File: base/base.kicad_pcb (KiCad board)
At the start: 2 copper layers, 105 x 100 mm, 22 parts, among them J1 FTDI, J2 CONN_01X04, J3 CONN_01X40, SW1 SW_Push, U1 Z80CPU, U2 27C256, U3 7404, U4 55257, U5 7432, U6 16550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

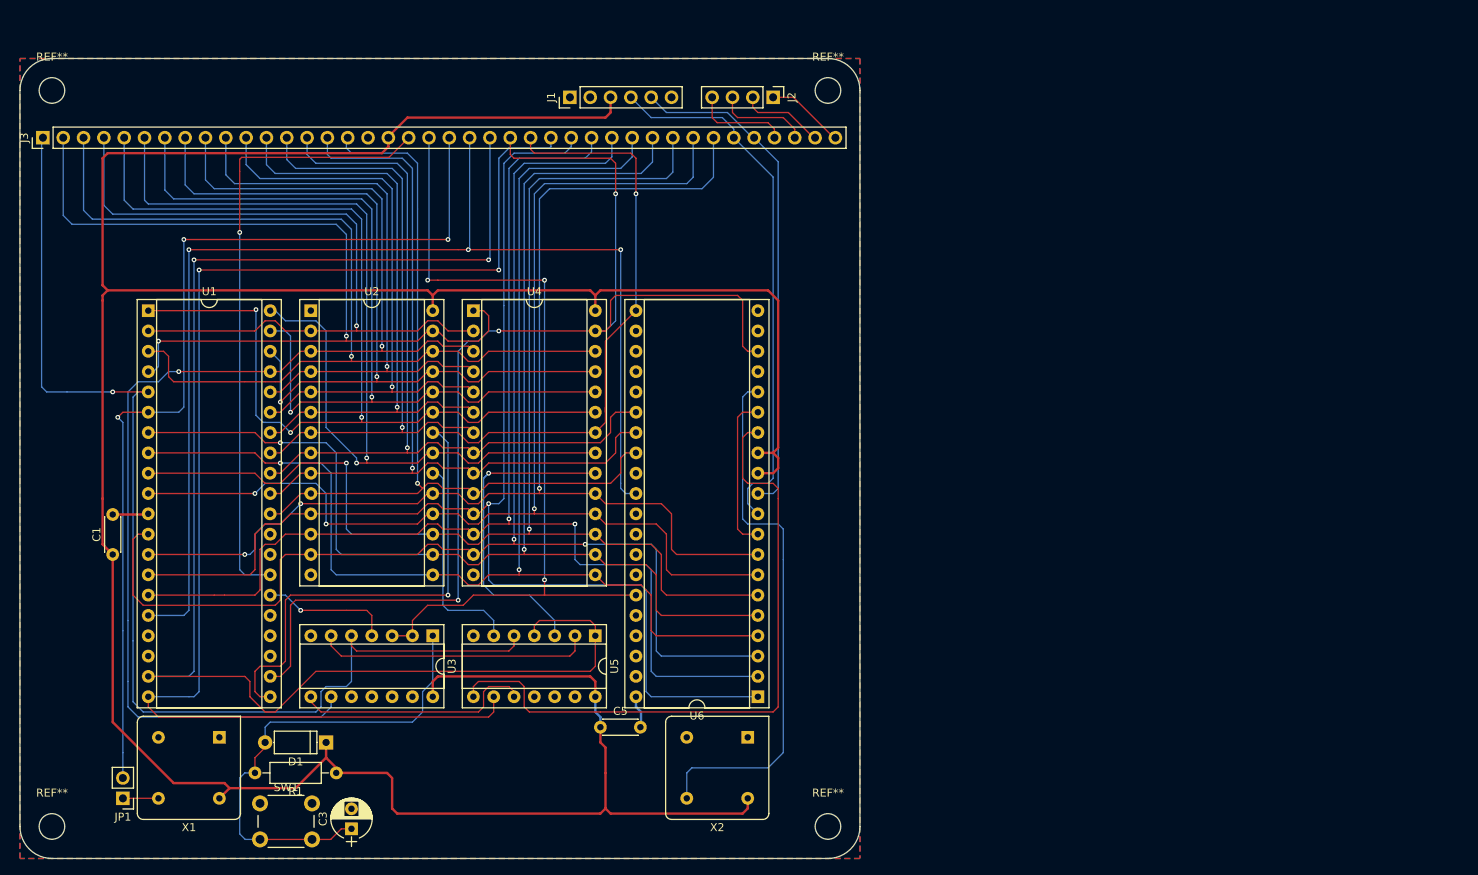
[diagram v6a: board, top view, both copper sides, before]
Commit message: Fixed silkscreen
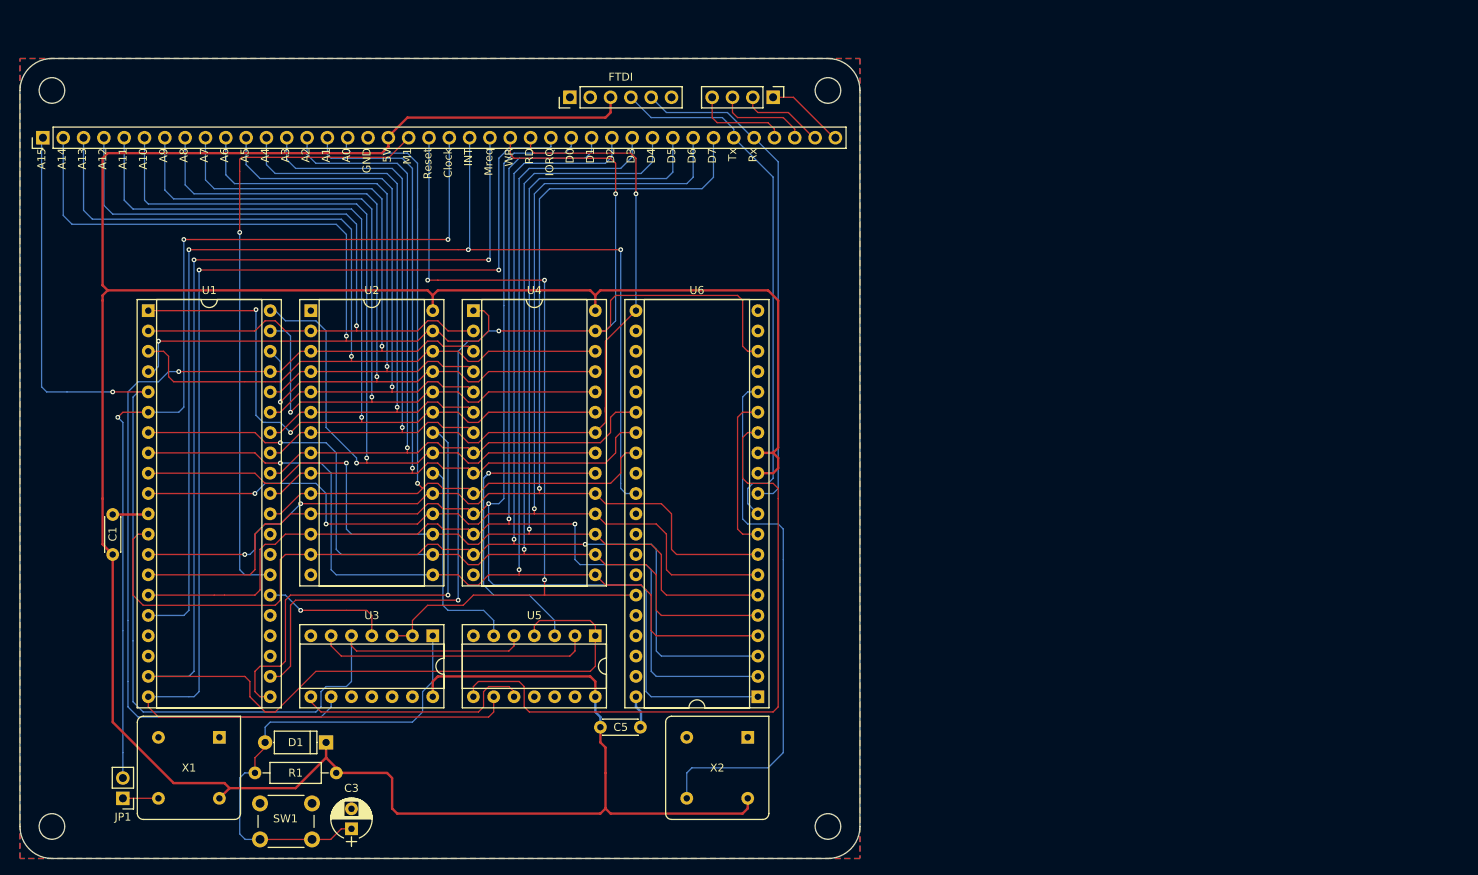
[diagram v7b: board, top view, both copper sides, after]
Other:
- board text added: "5V"
- board text added: "A0"
- board text added: "A1"
- board text added: "A10"
- board text added: "A11"
- board text added: "A12"
- board text added: "A13"
- board text added: "A14"
- board text added: "A15"
- board text added: "A2"
- board text added: "A3"
- board text added: "A4"
- board text added: "A5"
- board text added: "A6"
- board text added: "A7"
- board text added: "A8"
- board text added: "A9"
- board text added: "Clock"
- board text added: "D0"
- board text added: "D1"
- board text added: "D2"
- board text added: "D3"
- board text added: "D4"
- board text added: "D5"
- board text added: "D6"
- board text added: "D7"
- board text added: "GND"
- board text added: "INT"
- board text added: "IORQ"
- board text added: "M1"
- board text added: "Mreq"
- board text added: "RD"
- board text added: "Reset"
- board text added: "Rx"
- board text added: "Tx"
- board text added: "WR"

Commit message: Board layout for remaining pins
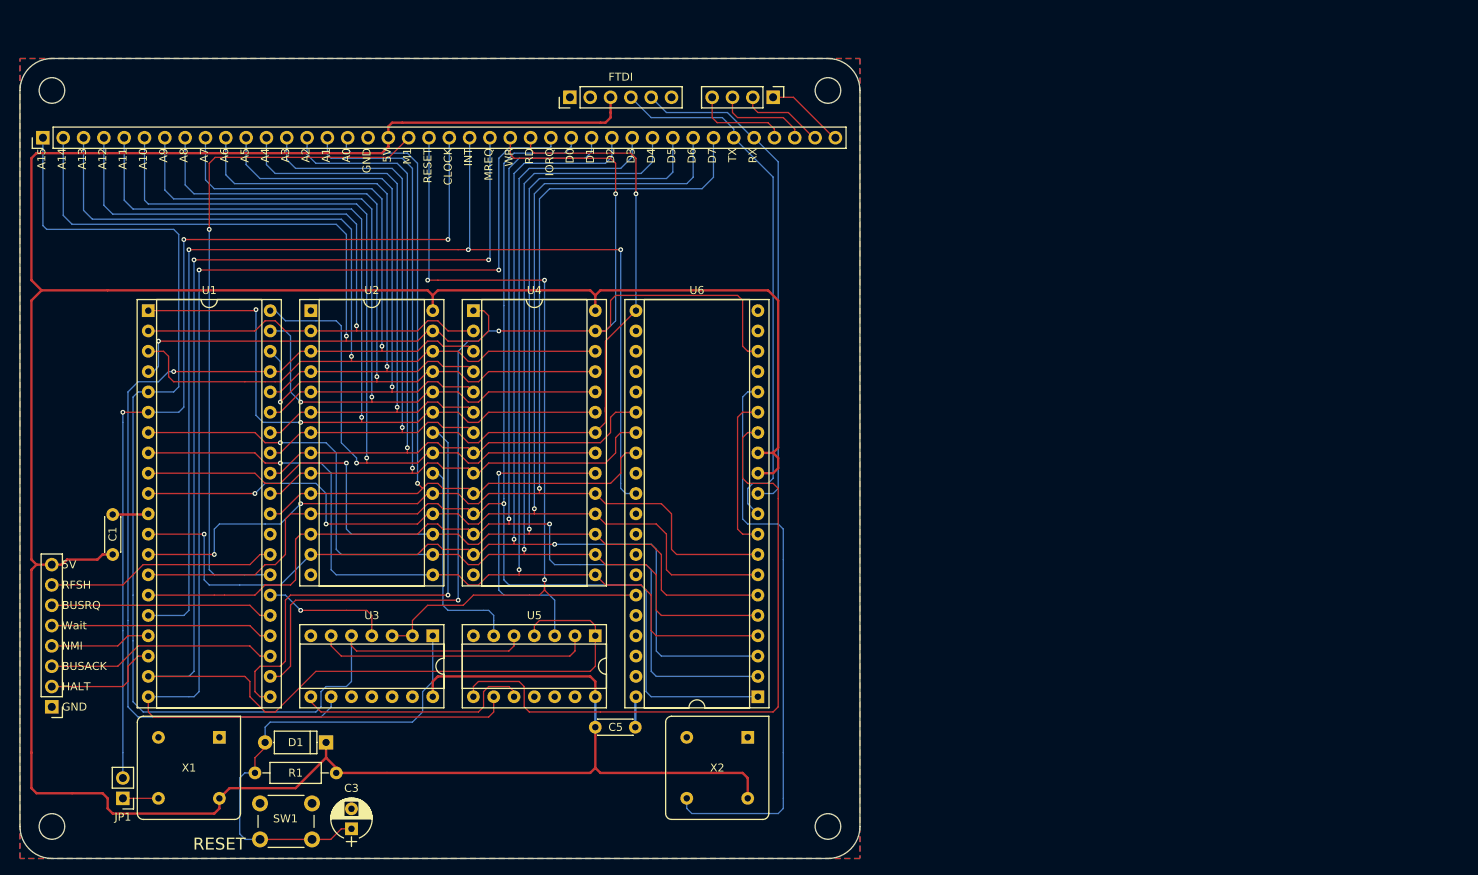
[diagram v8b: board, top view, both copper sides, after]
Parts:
- added J4: CONN_01X08, Pin_Headers:Pin_Header_Straight_1x08_Pitch2.54mm, F.Cu at (54.0, 146.1)
- added REF***: OSHW-Symbol_6.7x6mm_SilkScreen, Symbols:OSHW-Symbol_6.7x6mm_SilkScreen, B.Cu at (104.1, 156.2)
- moved C5 0.64 mm to (121.9, 148.6)
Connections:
- U1 pad 17: Net-(U1-Pad17) -> NMI
- U1 pad 18: Net-(U1-Pad18) -> HALT
- U1 pad 23: Net-(U1-Pad23) -> BUSACK
- U1 pad 24: Net-(U1-Pad24) -> WAIT
- U1 pad 25: Net-(U1-Pad25) -> BUSRQ
- U1 pad 28: Net-(U1-Pad28) -> RFSH
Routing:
- net +5V: track 390.4 -> 428.0 mm
- net RFSH: track 0.00 -> 28.9 mm
- net BUSACK: track 0.00 -> 28.9 mm
- net WAIT: track 0.00 -> 27.8 mm
- net BUSRQ: track 0.00 -> 27.8 mm
- net HALT: track 0.00 -> 14.8 mm
- net NMI: track 0.00 -> 12.6 mm
- net /D2: track 170.0 -> 160.4 mm, vias 2 -> 3
- net M1: track 77.6 -> 84.9 mm
- net /A15: track 145.3 -> 152.3 mm, vias 1 -> 0
- net Net-(U6-Pad16): track 67.2 -> 71.8 mm
- net /A9: track 111.3 -> 108.8 mm
- net RAM_CE: track 41.1 -> 38.6 mm
- net /D0: track 161.0 -> 159.5 mm
- net /A10: track 125.2 -> 126.7 mm
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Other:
- board text added: "BUSACK"
- board text added: "BUSRQ"
- board text added: "CLOCK"
- board text added: "HALT"
- board text added: "MREQ"
- board text added: "NMI"
- board text added: "RESET"
- board text added: "RFSH"
- board text added: "RX"
- board text added: "Rev. 1"
- board text added: "TX"
- board text added: "Wait"
- board text added: "Z80 Base https://github.com/Wiles/z80"
- board text removed: "Clock"
- board text removed: "Mreq"
- board text removed: "Reset"
- board text removed: "Rx"
- board text removed: "Tx"
